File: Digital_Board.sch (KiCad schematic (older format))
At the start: 0 parts

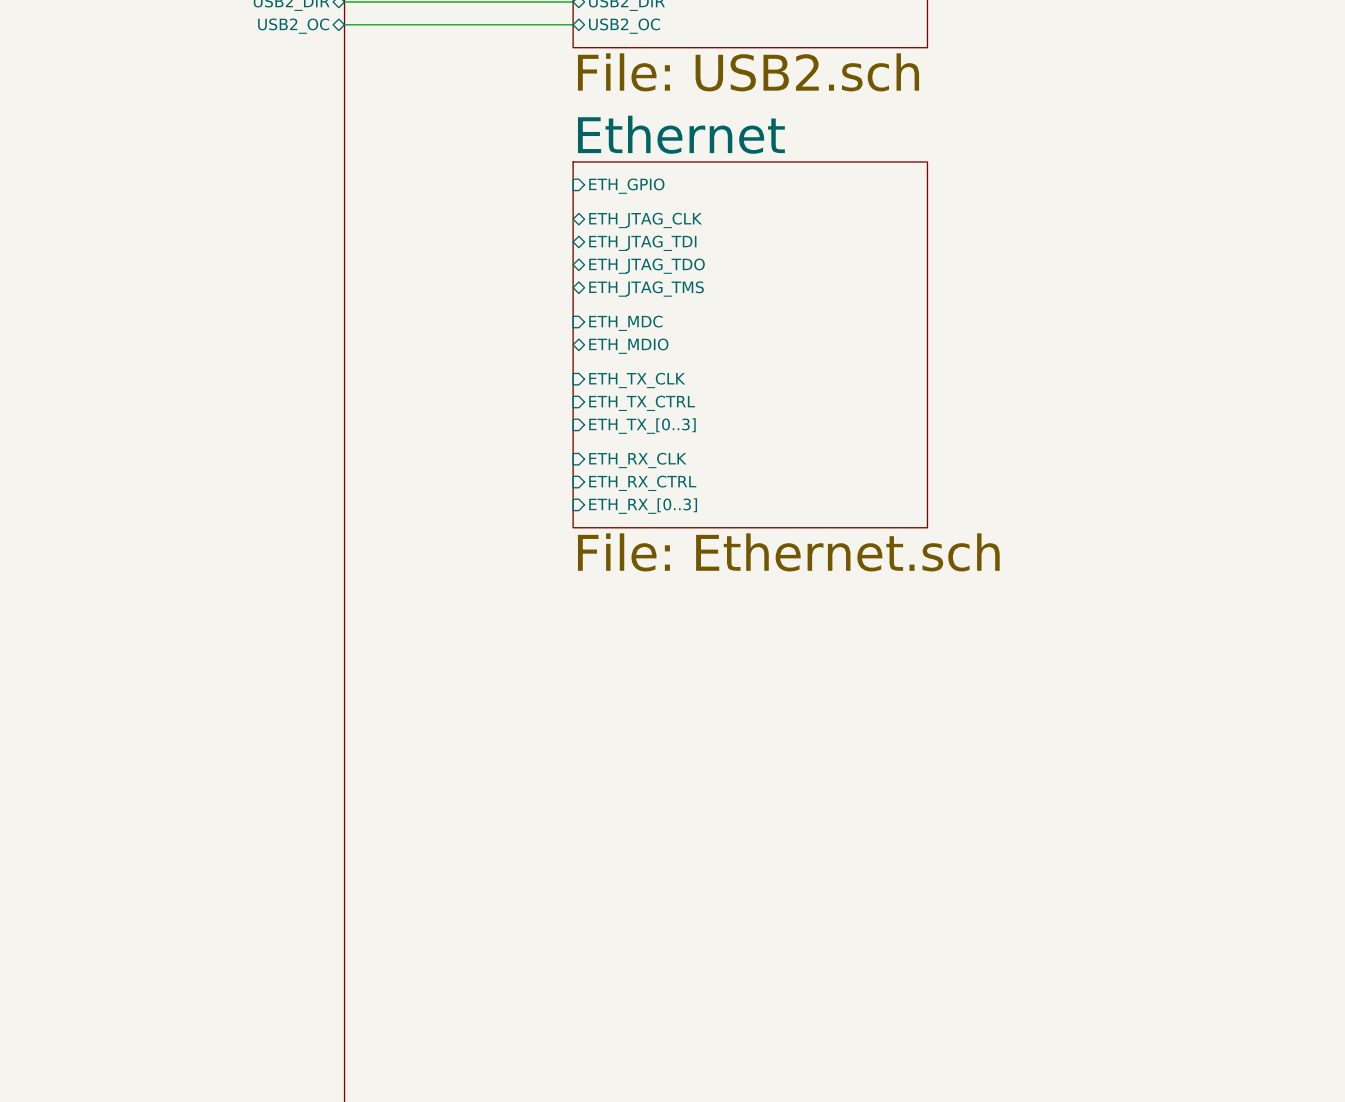
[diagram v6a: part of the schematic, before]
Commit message: Connected Ethernet sheet with FPGA bank
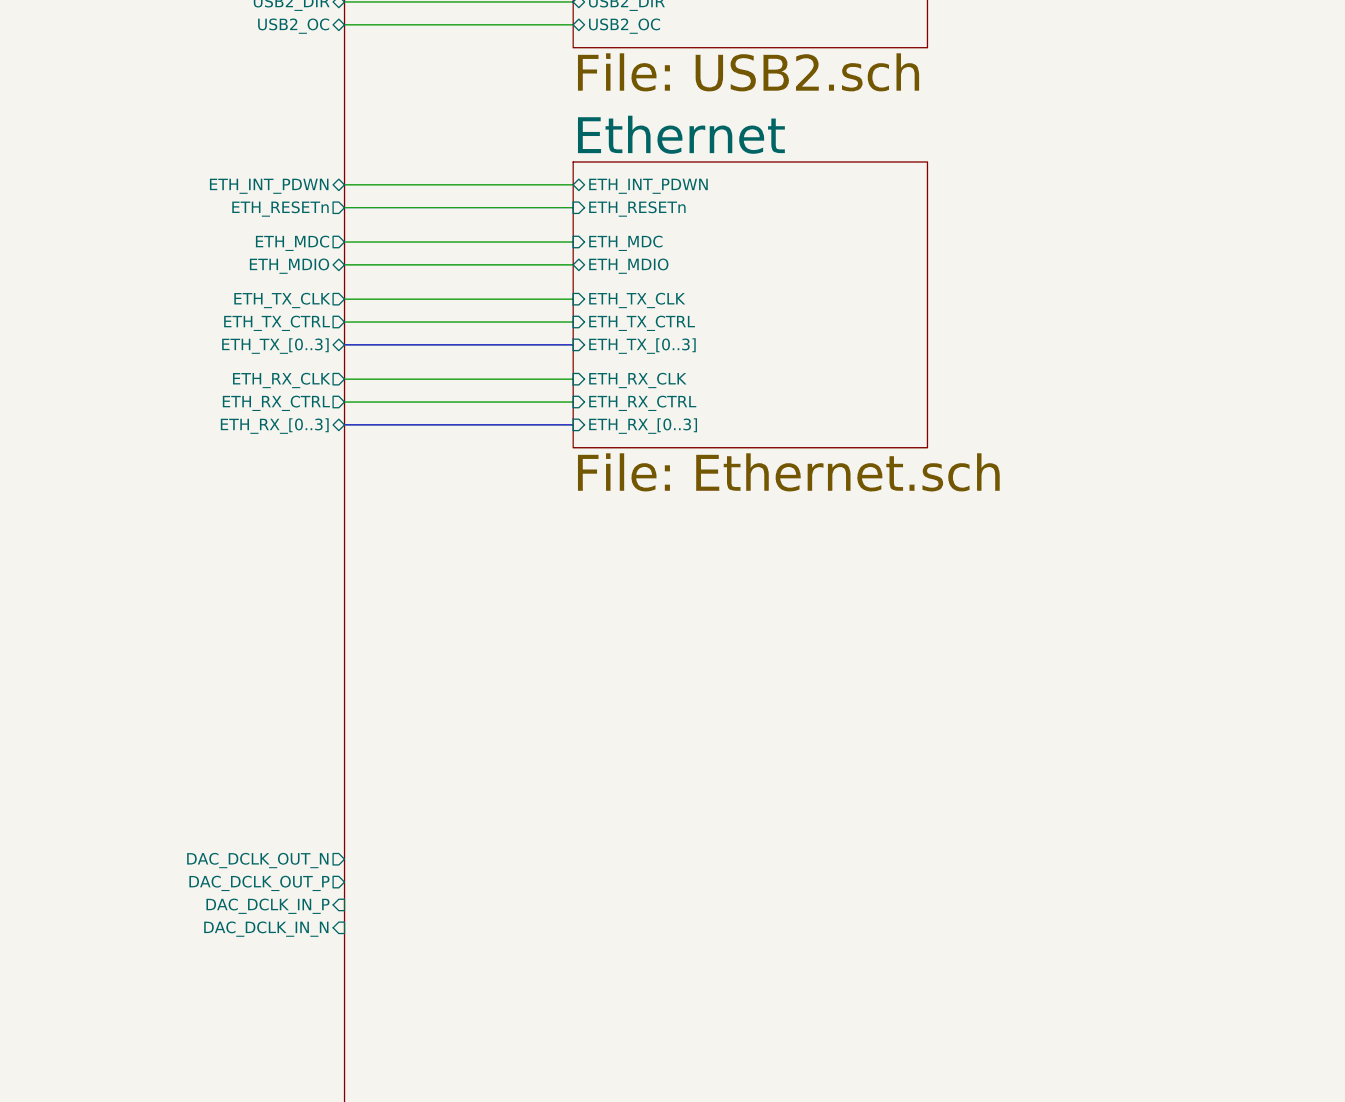
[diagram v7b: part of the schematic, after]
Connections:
- wire segments 44 -> 52
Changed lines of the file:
@@
-$EndSheet
-$Sheet
-S 15200 8600 1550 1600
-U 601E7C92
-F0 "Ethernet" 157
-F1 "Ethernet.sch" 157
-F2 "ETH_GPIO" I L 15200 8700 50
-F3 "ETH_JTAG_CLK" B L 15200 8850 50
-F4 "ETH_JTAG_TDI" B L 15200 8950 50
-F5 "ETH_JTAG_TDO" B L 15200 9050 50
-F6 "ETH_JTAG_TMS" B L 15200 9150 50
-F7 "ETH_MDC" I L 15200 9300 50
-F8 "ETH_MDIO" B L 15200 9400 50
-F9 "ETH_TX_CLK" I L 15200 9550 50
-F10 "ETH_TX_CTRL" I L 15200 9650 50
-F11 "ETH_TX_[0..3]" I L 15200 9750 50
-F12 "ETH_RX_[0..3]" I L 15200 10100 50
-F13 "ETH_RX_CLK" I L 15200 9900 50
-F14 "ETH_RX_CTRL" I L 15200 10000 50
 $EndSheet
 $Sheet
@@
 F1 "RS232_Port.sch" 50
 $EndSheet
+Text Label 3650 14750 0    50   ~ 0
+12V
+Wire Wire Line
+	21400 9800 20950 9800
+Text Label 21050 9800 0    50   ~ 0
+12V
+$Sheet
+S 15150 1600 1550 3200
+U 601E7AEB
+F0 "RAM" 157
+F1 "RAM.sch" 157
+F2 "DDR3_CK_P" I L 15150 1700 50
+F3 "DDR3_CK_N" I L 15150 1850 50
+F4 "DDR3_CKE0" I L 15150 2000 50
+F5 "DDR3_CS" I L 15150 2500 50
+F6 "DDR3_RAS" I L 15150 2700 50
+F7 "DDR3_CAS" I L 15150 2600 50
+F8 "DDR3_WE" I L 15150 2400 50
+F9 "DDR3_BA[0..2]" I L 15150 3100 50
+F10 "DDR3_A[0..14]" I L 15150 2950 50
+F11 "DDR3_VREF" B L 15150 3250 50
+F12 "DDR3_RESET" I L 15150 2800 50
+F13 "DDR3_ODT0" I L 15150 3450 50
+F14 "DDR3_DM1" I L 15150 3600 50
+F15 "DDR3_DM0" I L 15150 3700 50
+F16 "DDR3_DM3" I L 15150 3800 50
+F17 "DDR3_DM2" I L 15150 3900 50
+F18 "DDR3_DQS0_N" B L 15150 4000 50
+F19 "DDR3_DQS0_P" B L 15150 4100 50
+F20 "DDR3_DQS1_N" B L 15150 4200 50
+F21 "DDR3_DQS1_P" B L 15150 4300 50
+F22 "DDR3_DQS2_N" B L 15150 4400 50
+F23 "DDR3_DQS2_P" B L 15150 4500 50
+F24 "DDR3_DQS3_N" B L 15150 4600 50
+F25 "DDR3_DQS3_P" B L 15150 4700 50
+F26 "DDR3_D[0..15]" B L 15150 2150 50
+F27 "DDR3_D[16..31]" B L 15150 2250 50
+$EndSheet
+Wire Wire Line
+	15150 3250 14200 3250
+Wire Wire Line
+	15150 4700 14200 4700
+Wire Wire Line
+	15150 4600 14200 4600
+Wire Wire Line
+	15150 4500 14200 4500
+Wire Wire Line
+	15150 4400 14200 4400
+Wire Wire Line
+	14200 4300 15150 4300
+Wire Wire Line
+	15150 4200 14200 4200
+Wire Wire Line
+	14200 4100 15150 4100
+Wire Wire Line
+	15150 4000 14200 4000
+Wire Wire Line
+	15150 3900 14200 3900
+Wire Wire Line
+	15150 3800 14200 3800
+Wire Wire Line
+	15150 3700 14200 3700
+Wire Wire Line
+	14200 3450 15150 3450
+Wire Wire Line
+	14200 3600 15150 3600
+Wire Wire Line
+	14200 1700 15150 1700
+Wire Wire Line
+	15150 1850 14200 1850
+Wire Wire Line
+	14200 2000 15150 2000
+Wire Bus Line
+	15150 2150 14200 2150
+Wire Bus Line
+	14200 2250 15150 2250
+Wire Wire Line
+	15150 2800 14200 2800
+Wire Wire Line
+	14200 2700 15150 2700
+Wire Wire Line
+	15150 2600 14200 2600
+Wire Wire Line
+	14200 2500 15150 2500
+Wire Wire Line
+	15150 2400 14200 2400
+Wire Bus Line
+	15150 2950 14200 2950
+Wire Bus Line
+	15150 3100 14200 3100
+Wire Wire Line
+	14200 5400 15200 5400
+Wire Wire Line
+	14200 5500 15200 5500
+Wire Wire Line
+	14200 5600 15200 5600
+Wire Wire Line
+	14200 5700 15200 5700
+Wire Wire Line
+	14200 5800 15200 5800
+Wire Wire Line
+	14200 5900 15200 5900
+Wire Wire Line
+	14200 6000 15200 6000
+Wire Wire Line
+	14200 6100 15200 6100
+Wire Wire Line
+	14200 6200 15200 6200
+Wire Wire Line
+	14200 6300 15200 6300
+Wire Wire Line
+	14200 6400 15200 6400
+Wire Wire Line
+	14200 6500 15200 6500
+Wire Wire Line
+	14200 6600 15200 6600
+Wire Wire Line
+	14200 6700 15200 6700
+Wire Bus Line
+	15200 7500 14200 7500
+Wire Wire Line
+	15200 7400 14200 7400
+Wire Wire Line
+	14200 7600 15200 7600
+Wire Wire Line
+	15200 7700 14200 7700
+Wire Wire Line
+	14200 7800 15200 7800
+Wire Wire Line
+	15200 7900 14200 7900
+Wire Wire Line
+	14200 8000 15200 8000
+Text Notes 15850 950  0    157  ~ 0
+put filter beads for all power supplies at each circuit
+Wire Bus Line
+	15200 9400 14200 9400
+Wire Bus Line
+	14200 9750 15200 9750
+$Sheet
+S 15200 8600 1550 1250
+U 601E7C92
+F0 "Ethernet" 157
+F1 "Ethernet.sch" 157
+F2 "ETH_MDC" I L 15200 8950 50
+F3 "ETH_MDIO" B L 15200 9050 50
+F4 "ETH_TX_CLK" I L 15200 9200 50
+F5 "ETH_TX_CTRL" I L 15200 9300 50
+F6 "ETH_TX_[0..3]" I L 15200 9400 50
+F7 "ETH_RX_[0..3]" I L 15200 9750 50
+F8 "ETH_RX_CLK" I L 15200 9550 50
+F9 "ETH_RX_CTRL" I L 15200 9650 50
+F10 "ETH_INT_PDWN" B L 15200 8700 50
+F11 "ETH_RESETn" I L 15200 8800 50
+$EndSheet
+Wire Wire Line
+	14200 9550 15200 9550
+Wire Wire Line
+	15200 9650 14200 9650
+Wire Wire Line
+	14200 9300 15200 9300
+Wire Wire Line
+	15200 9200 14200 9200
+Wire Wire Line
+	15200 8950 14200 8950
+Wire Wire Line
+	14200 9050 15200 9050
+Wire Wire Line
+	14200 8800 15200 8800
+Wire Wire Line
+	15200 8700 14200 8700
 $Sheet
 S 11650 750  2550 14250
@@
 F47 "USB2_RESTN" B R 14200 7600 50
 F48 "USB2_OC" B R 14200 8000 50
-$EndSheet
-Text Label 3650 14750 0    50   ~ 0
-12V
-Wire Wire Line
-	21400 9800 20950 9800
-Text Label 21050 9800 0    50   ~ 0
-12V
-$Sheet
-S 15150 1600 1550 3200
-U 601E7AEB
-F0 "RAM" 157
-F1 "RAM.sch" 157
-F2 "DDR3_CK_P" I L 15150 1700 50
-F3 "DDR3_CK_N" I L 15150 1850 50
-F4 "DDR3_CKE0" I L 15150 2000 50
-F5 "DDR3_CS" I L 15150 2500 50
-F6 "DDR3_RAS" I L 15150 2700 50
-F7 "DDR3_CAS" I L 15150 2600 50
-F8 "DDR3_WE" I L 15150 2400 50
-F9 "DDR3_BA[0..2]" I L 15150 3100 50
-F10 "DDR3_A[0..14]" I L 15150 2950 50
-F11 "DDR3_VREF" B L 15150 3250 50
-F12 "DDR3_RESET" I L 15150 2800 50
-F13 "DDR3_ODT0" I L 15150 3450 50
-F14 "DDR3_DM1" I L 15150 3600 50
-F15 "DDR3_DM0" I L 15150 3700 50
-F16 "DDR3_DM3" I L 15150 3800 50
-F17 "DDR3_DM2" I L 15150 3900 50
-F18 "DDR3_DQS0_N" B L 15150 4000 50
-F19 "DDR3_DQS0_P" B L 15150 4100 50
-F20 "DDR3_DQS1_N" B L 15150 4200 50
-F21 "DDR3_DQS1_P" B L 15150 4300 50
-F22 "DDR3_DQS2_N" B L 15150 4400 50
-F23 "DDR3_DQS2_P" B L 15150 4500 50
-F24 "DDR3_DQS3_N" B L 15150 4600 50
-F25 "DDR3_DQS3_P" B L 15150 4700 50
-F26 "DDR3_D[0..15]" B L 15150 2150 50
-F27 "DDR3_D[16..31]" B L 15150 2250 50
-$EndSheet
-Wire Wire Line
-	15150 3250 14200 3250
-Wire Wire Line
-	15150 4700 14200 4700
-Wire Wire Line
-	15150 4600 14200 4600
-Wire Wire Line
-	15150 4500 14200 4500
-Wire Wire Line
-	15150 4400 14200 4400
-Wire Wire Line
-	14200 4300 15150 4300
-Wire Wire Line
-	15150 4200 14200 4200
-Wire Wire Line
-	14200 4100 15150 4100
-Wire Wire Line
-	15150 4000 14200 4000
-Wire Wire Line
-	15150 3900 14200 3900
-Wire Wire Line
-	15150 3800 14200 3800
-Wire Wire Line
-	15150 3700 14200 3700
-Wire Wire Line
-	14200 3450 15150 3450
-Wire Wire Line
-	14200 3600 15150 3600
-Wire Wire Line
-	14200 1700 15150 1700
-Wire Wire Line
-	15150 1850 14200 1850
-Wire Wire Line
-	14200 2000 15150 2000
-Wire Bus Line
-	15150 2150 14200 2150
-Wire Bus Line
-	14200 2250 15150 2250
-Wire Wire Line
-	15150 2800 14200 2800
-Wire Wire Line
-	14200 2700 15150 2700
-Wire Wire Line
-	15150 2600 14200 2600
-Wire Wire Line
-	14200 2500 15150 2500
-Wire Wire Line
-	15150 2400 14200 2400
-Wire Bus Line
-	15150 2950 14200 2950
-Wire Bus Line
-	15150 3100 14200 3100
-Wire Wire Line
-	14200 5400 15200 5400
-Wire Wire Line
-	14200 5500 15200 5500
-Wire Wire Line
-	14200 5600 15200 5600
-Wire Wire Line
-	14200 5700 15200 5700
-Wire Wire Line
-	14200 5800 15200 5800
-Wire Wire Line
-	14200 5900 15200 5900
-Wire Wire Line
-	14200 6000 15200 6000
-Wire Wire Line
-	14200 6100 15200 6100
-Wire Wire Line
-	14200 6200 15200 6200
-Wire Wire Line
-	14200 6300 15200 6300
-Wire Wire Line
-	14200 6400 15200 6400
-Wire Wire Line
-	14200 6500 15200 6500
-Wire Wire Line
-	14200 6600 15200 6600
-Wire Wire Line
-	14200 6700 15200 6700
-Wire Bus Line
-	15200 7500 14200 7500
-Wire Wire Line
-	15200 7400 14200 7400
-Wire Wire Line
-	14200 7600 15200 7600
-Wire Wire Line
-	15200 7700 14200 7700
-Wire Wire Line
-	14200 7800 15200 7800
-Wire Wire Line
-	15200 7900 14200 7900
-Wire Wire Line
-	14200 8000 15200 8000
-Text Notes 15850 950  0    157  ~ 0
-put filter beads for all power supplies at each circuit
+F49 "DAC_DCLK_OUT_P" O R 14200 11750 50
+F50 "DAC_DCLK_OUT_N" O R 14200 11650 50
+F51 "DAC_DCLK_IN_P" I R 14200 11850 50
+F52 "DAC_DCLK_IN_N" I R 14200 11950 50
+F53 "ETH_TX_CLK" O R 14200 9200 50
+F54 "ETH_TX_CTRL" O R 14200 9300 50
+F55 "ETH_TX_[0..3]" B R 14200 9400 50
+F56 "ETH_RX_CLK" O R 14200 9550 50
+F57 "ETH_RX_CTRL" O R 14200 9650 50
+F58 "ETH_RX_[0..3]" B R 14200 9750 50
+F59 "ETH_MDIO" B R 14200 9050 50
+F60 "ETH_MDC" O R 14200 8950 50
+F61 "ETH_INT_PDWN" B R 14200 8700 50
+F62 "ETH_RESETn" O R 14200 8800 50
+$EndSheet
 $EndSCHEMATC

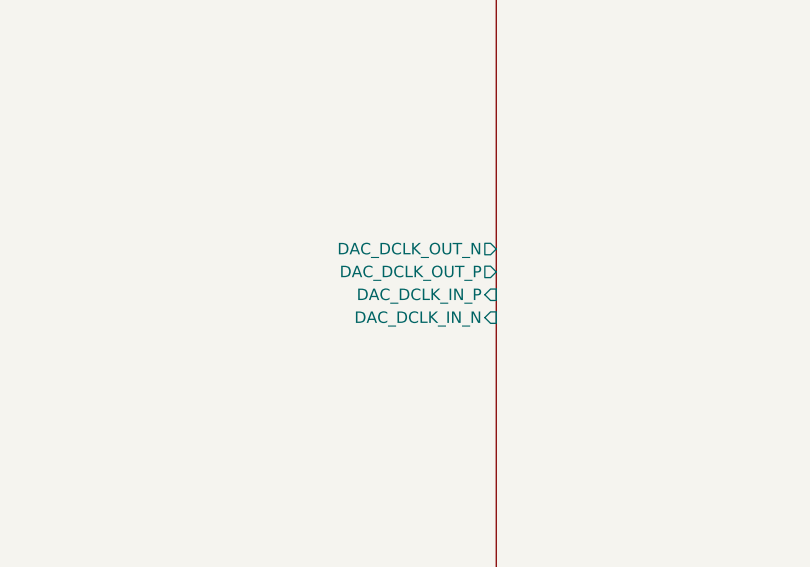
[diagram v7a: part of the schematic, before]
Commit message: PCB created and schematics annotated High speed connections added to the BTB
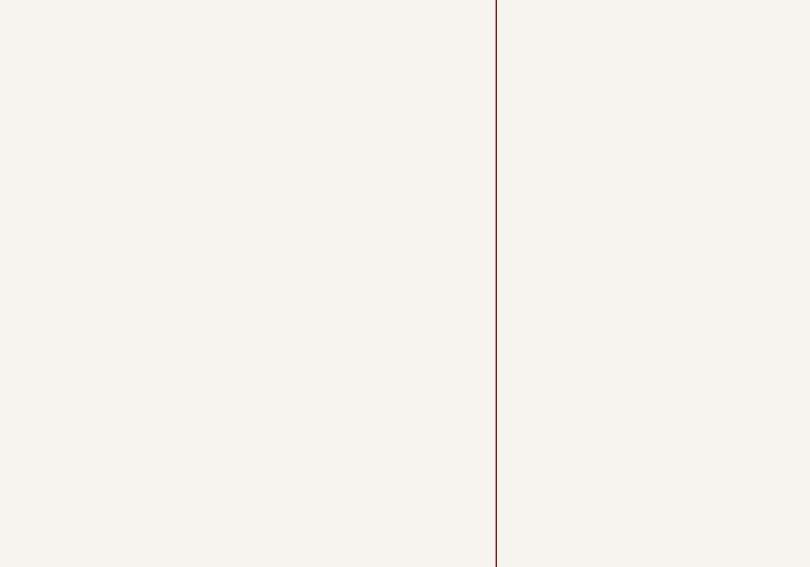
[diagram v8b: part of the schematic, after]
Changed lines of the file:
@@
 F47 "USB2_RESTN" B R 14200 7600 50
 F48 "USB2_OC" B R 14200 8000 50
-F49 "DAC_DCLK_OUT_P" O R 14200 11750 50
-F50 "DAC_DCLK_OUT_N" O R 14200 11650 50
-F51 "DAC_DCLK_IN_P" I R 14200 11850 50
-F52 "DAC_DCLK_IN_N" I R 14200 11950 50
-F53 "ETH_TX_CLK" O R 14200 9200 50
-F54 "ETH_TX_CTRL" O R 14200 9300 50
-F55 "ETH_TX_[0..3]" B R 14200 9400 50
-F56 "ETH_RX_CLK" O R 14200 9550 50
-F57 "ETH_RX_CTRL" O R 14200 9650 50
-F58 "ETH_RX_[0..3]" B R 14200 9750 50
-F59 "ETH_MDIO" B R 14200 9050 50
-F60 "ETH_MDC" O R 14200 8950 50
-F61 "ETH_INT_PDWN" B R 14200 8700 50
-F62 "ETH_RESETn" O R 14200 8800 50
+F49 "ETH_TX_CLK" O R 14200 9200 50
+F50 "ETH_TX_CTRL" O R 14200 9300 50
+F51 "ETH_TX_[0..3]" B R 14200 9400 50
+F52 "ETH_RX_CLK" O R 14200 9550 50
+F53 "ETH_RX_CTRL" O R 14200 9650 50
+F54 "ETH_RX_[0..3]" B R 14200 9750 50
+F55 "ETH_MDIO" B R 14200 9050 50
+F56 "ETH_MDC" O R 14200 8950 50
+F57 "ETH_INT_PDWN" B R 14200 8700 50
+F58 "ETH_RESETn" O R 14200 8800 50
 $EndSheet
 $EndSCHEMATC
